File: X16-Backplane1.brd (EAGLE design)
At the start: 131.3 x 109.7 mm, 26 parts, among them J1 CONN_PXC-8-RA-1778683, J12 282837-3, J13 282837-3, J2 CONN_ET60S-D04-3-08-D04-X-R1-S, J3 HTST-110-04-L-D-RA, J4 CLT-110-01-F-D, U2 TRANS_ULN2003AD

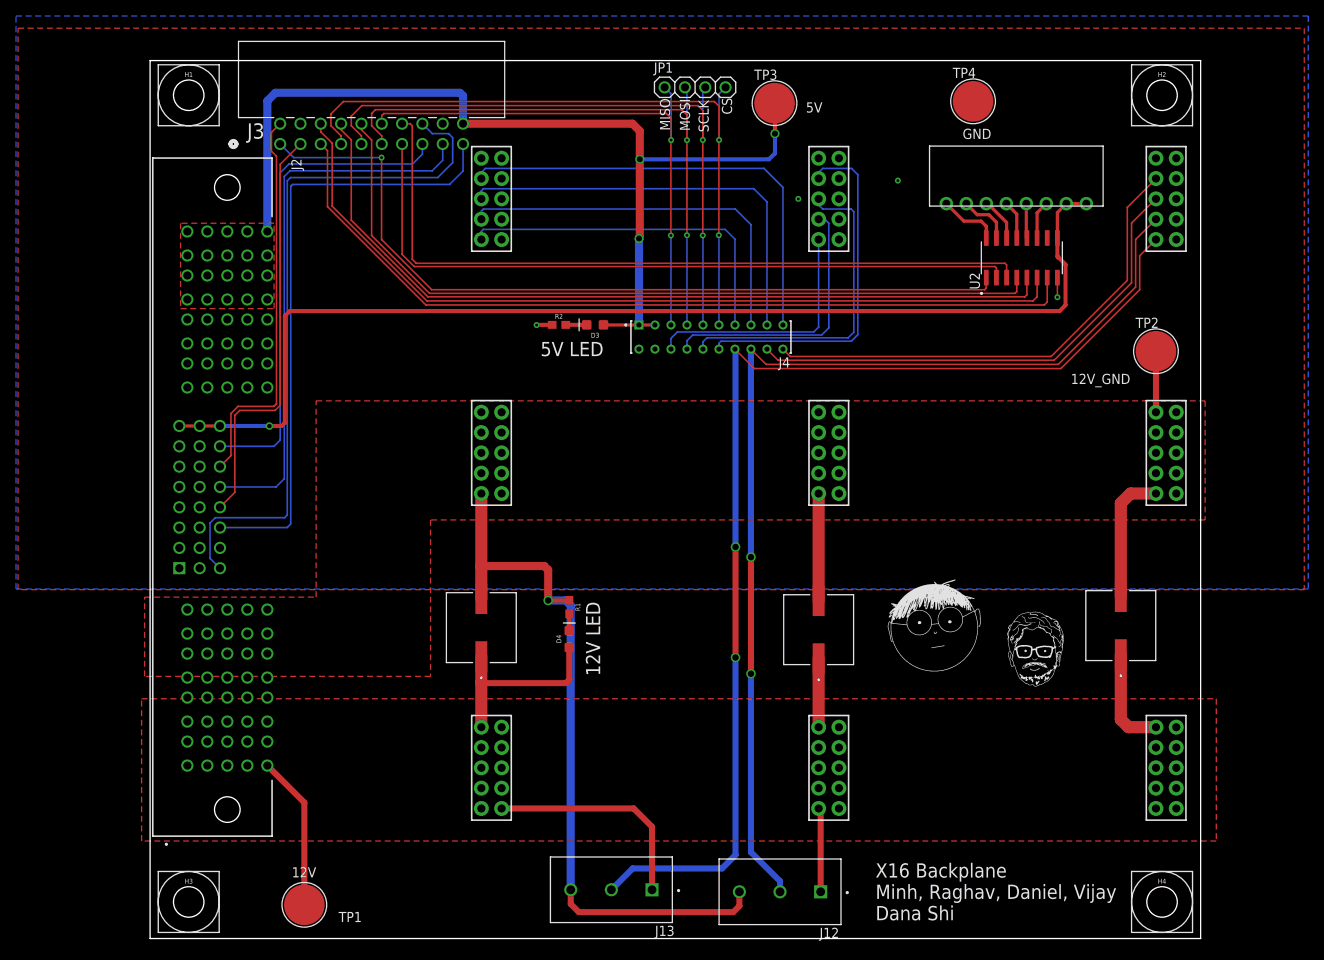
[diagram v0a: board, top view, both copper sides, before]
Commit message: Revert "Minh Update 4"
This reverts commit 6540dcb78246fca95661c726553611ac5071b16d.
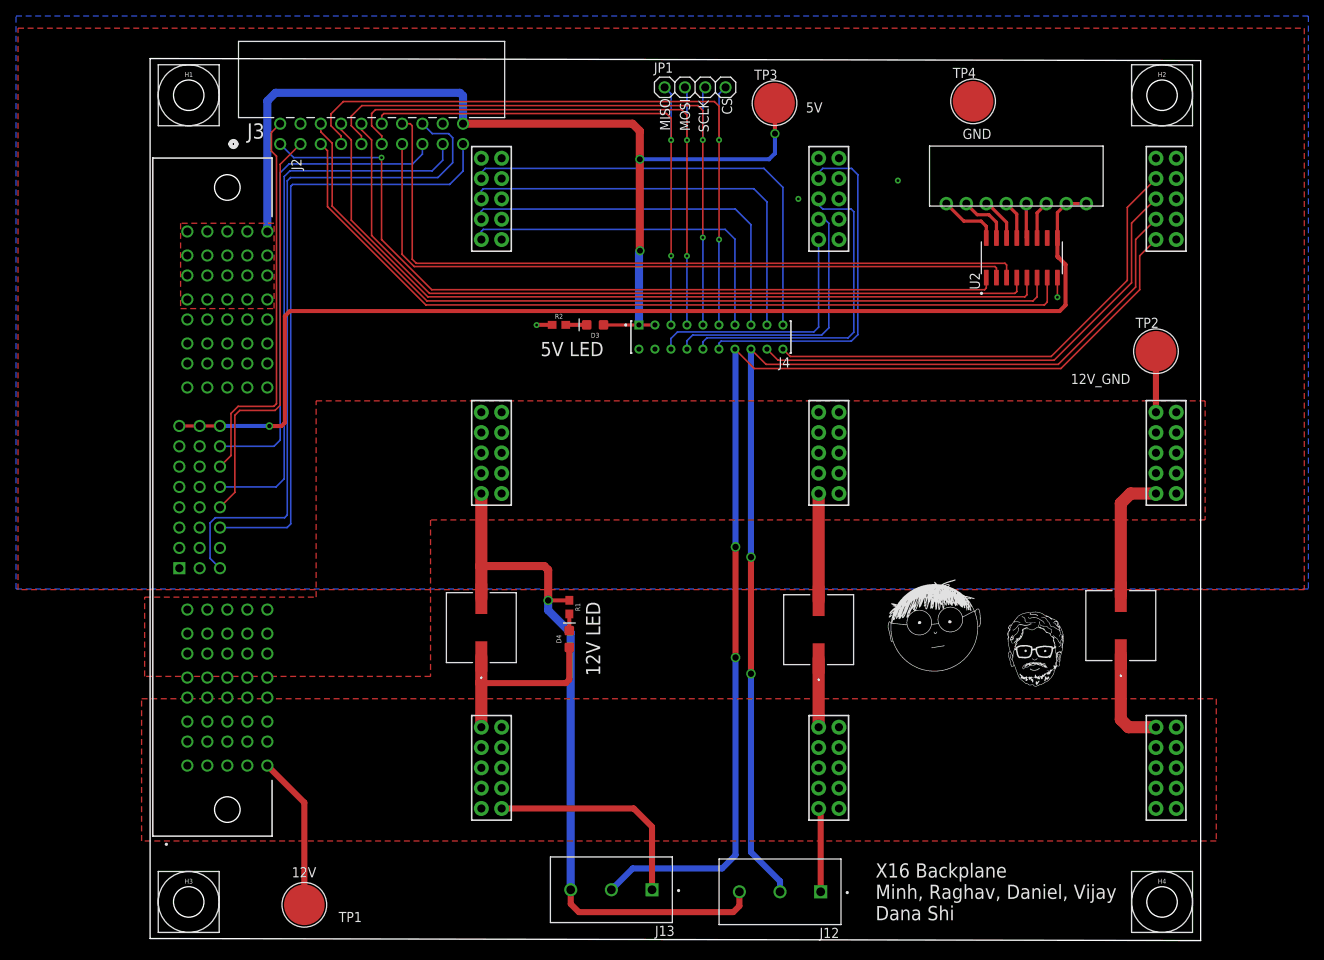
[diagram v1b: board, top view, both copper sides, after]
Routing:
- net 12V_GND: track 129.8 -> 128.5 mm
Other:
- board size 131.3 x 109.7 mm -> 131.3 x 110.3 mm
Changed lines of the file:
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@@
 <board>
 <plain>
-<wire x1="0" y1="0" x2="131.318" y2="0" width="0" layer="20"/>
-<wire x1="131.318" y1="0" x2="131.318" y2="109.746" width="0" layer="20"/>
-<wire x1="131.318" y1="109.746" x2="0" y2="109.746" width="0" layer="20"/>
-<wire x1="0" y1="109.746" x2="0" y2="0" width="0" layer="20"/>
+<wire x1="0" y1="0" x2="131.318" y2="-0.254" width="0" layer="20"/>
+<wire x1="131.318" y1="-0.254" x2="131.318" y2="109.746" width="0" layer="20"/>
+<wire x1="131.318" y1="109.746" x2="0" y2="110" width="0" layer="20"/>
+<wire x1="0" y1="110" x2="0" y2="0" width="0" layer="20"/>
 <polygon width="0.4064" layer="29">
 <vertex x="23.368" y="56.388"/>
@@
 <wire x1="41.402" y1="55.626" x2="41.402" y2="46.5582" width="1.524" layer="1"/>
 <wire x1="125.73" y1="65.786" x2="125.73" y2="73.406" width="0.762" layer="1"/>
-<wire x1="52.578" y1="6.096" x2="52.578" y2="41.6306" width="1.016" layer="16"/>
+<wire x1="52.578" y1="6.096" x2="52.578" y2="38.2016" width="1.016" layer="16"/>
+<wire x1="49.7586" y1="41.021" x2="49.7586" y2="42.2656" width="1.016" layer="16"/>
 <via x="49.7586" y="42.2656" extent="1-16" drill="0.8"/>
-<wire x1="52.578" y1="41.6306" x2="51.943" y2="42.2656" width="1.016" layer="16"/>
-<wire x1="49.7586" y1="42.2656" x2="51.943" y2="42.2656" width="1.016" layer="16"/>
+<wire x1="52.578" y1="38.2016" x2="49.7586" y2="41.021" width="1.016" layer="16"/>
 <wire x1="49.7586" y1="42.2656" x2="49.7586" y2="46.0756" width="1.016" layer="1"/>
 <wire x1="49.7586" y1="46.0756" x2="49.276" y2="46.5582" width="1.016" layer="1"/>
@@
 <wire x1="61.214" y1="100.9396" x2="61.214" y2="97.409" width="1.016" layer="1"/>
 <via x="61.214" y="97.409" extent="1-16" drill="0.75"/>
-<wire x1="61.214" y1="97.409" x2="61.214" y2="87.6046" width="1.016" layer="1"/>
-<wire x1="61.214" y1="87.6046" x2="61.1124" y2="87.503" width="1.016" layer="1"/>
-<via x="61.1124" y="87.503" extent="1-16" drill="0.75"/>
-<wire x1="61.1124" y1="87.503" x2="61.1124" y2="76.7024" width="1.016" layer="16"/>
+<wire x1="61.214" y1="97.409" x2="61.214" y2="86.0044" width="1.016" layer="1"/>
+<wire x1="61.214" y1="86.0044" x2="61.2394" y2="85.979" width="1.016" layer="1"/>
+<via x="61.2394" y="85.979" extent="1-16" drill="0.75"/>
+<wire x1="61.2394" y1="85.979" x2="61.1124" y2="85.852" width="1.016" layer="16"/>
+<wire x1="61.1124" y1="85.852" x2="61.1124" y2="76.7024" width="1.016" layer="16"/>
 <wire x1="61.1124" y1="76.7024" x2="61.104" y2="76.694" width="1.016" layer="16"/>
 <wire x1="61.214" y1="97.409" x2="77.3684" y2="97.409" width="0.508" layer="16"/>
@@
 <contactref element="J4" pad="05"/>
 <contactref element="J3" pad="12"/>
-<wire x1="65.104" y1="76.694" x2="65.104" y2="87.8802" width="0.2032" layer="16"/>
-<wire x1="65.104" y1="87.8802" x2="65.1002" y2="87.884" width="0.2032" layer="16"/>
-<via x="65.1002" y="87.884" extent="1-16" drill="0.35"/>
-<wire x1="65.1002" y1="99.7712" x2="65.1256" y2="99.7966" width="0.2032" layer="1"/>
-<wire x1="65.1002" y1="99.7712" x2="65.1002" y2="87.884" width="0.2032" layer="1"/>
+<wire x1="65.104" y1="76.694" x2="65.104" y2="85.3224" width="0.2032" layer="16"/>
+<wire x1="65.104" y1="85.3224" x2="65.1256" y2="85.344" width="0.2032" layer="16"/>
+<via x="65.1256" y="85.344" extent="1-16" drill="0.35"/>
+<wire x1="65.1256" y1="85.344" x2="65.1256" y2="99.7966" width="0.2032" layer="1"/>
 <wire x1="65.1256" y1="99.7966" x2="65.1256" y2="102.5398" width="0.2032" layer="1"/>
 <wire x1="65.1256" y1="102.5398" x2="64.5414" y2="103.124" width="0.2032" layer="1"/>
@@
 <contactref element="J4" pad="07"/>
 <contactref element="J3" pad="11"/>
-<wire x1="67.104" y1="76.694" x2="67.104" y2="87.9066" width="0.2032" layer="16"/>
-<wire x1="67.104" y1="87.9066" x2="67.1068" y2="87.9094" width="0.2032" layer="16"/>
-<via x="67.1068" y="87.9094" extent="1-16" drill="0.35"/>
-<wire x1="67.1068" y1="87.9094" x2="67.1068" y2="99.7966" width="0.2032" layer="1"/>
+<wire x1="67.104" y1="76.694" x2="67.104" y2="85.3158" width="0.2032" layer="16"/>
+<wire x1="67.104" y1="85.3158" x2="67.1068" y2="85.3186" width="0.2032" layer="16"/>
+<via x="67.1068" y="85.3186" extent="1-16" drill="0.35"/>
+<wire x1="67.1068" y1="85.3186" x2="67.1068" y2="99.7966" width="0.2032" layer="1"/>
 <wire x1="67.1068" y1="99.7966" x2="67.1068" y2="102.9462" width="0.2032" layer="1"/>
 <wire x1="67.1068" y1="102.9462" x2="66.4464" y2="103.6066" width="0.2032" layer="1"/>
@@
 <contactref element="J4" pad="09"/>
 <contactref element="J3" pad="9"/>
-<wire x1="69.104" y1="76.694" x2="69.104" y2="87.868" width="0.2032" layer="16"/>
-<wire x1="69.104" y1="87.868" x2="69.088" y2="87.884" width="0.2032" layer="16"/>
-<via x="69.088" y="87.884" extent="1-16" drill="0.35"/>
-<wire x1="69.088" y1="87.884" x2="69.088" y2="99.822" width="0.2032" layer="1"/>
+<wire x1="69.104" y1="76.694" x2="69.104" y2="87.614" width="0.2032" layer="16"/>
+<wire x1="69.104" y1="87.614" x2="69.088" y2="87.63" width="0.2032" layer="16"/>
+<via x="69.088" y="87.63" extent="1-16" drill="0.35"/>
+<wire x1="69.088" y1="87.63" x2="69.088" y2="99.822" width="0.2032" layer="1"/>
 <wire x1="69.088" y1="99.822" x2="69.088" y2="103.505" width="0.2032" layer="1"/>
 <wire x1="69.088" y1="103.505" x2="68.4784" y2="104.1146" width="0.2032" layer="1"/>
@@
 <contactref element="J4" pad="11"/>
 <contactref element="J3" pad="7"/>
-<wire x1="71.104" y1="76.694" x2="71.104" y2="87.9" width="0.2032" layer="16"/>
-<wire x1="71.104" y1="87.9" x2="71.0946" y2="87.9094" width="0.2032" layer="16"/>
-<via x="71.0946" y="87.9094" extent="1-16" drill="0.35"/>
-<wire x1="71.0946" y1="99.7966" x2="71.12" y2="99.822" width="0.2032" layer="1"/>
-<wire x1="71.0946" y1="99.7966" x2="71.0946" y2="87.9094" width="0.2032" layer="1"/>
+<wire x1="71.104" y1="76.694" x2="71.104" y2="87.36" width="0.2032" layer="16"/>
+<wire x1="71.104" y1="87.36" x2="71.12" y2="87.376" width="0.2032" layer="16"/>
+<via x="71.12" y="87.376" extent="1-16" drill="0.35"/>
+<wire x1="71.12" y1="87.376" x2="71.12" y2="99.822" width="0.2032" layer="1"/>
 <wire x1="71.12" y1="99.822" x2="71.12" y2="104.0384" width="0.2032" layer="1"/>
 <wire x1="70.5358" y1="104.6226" x2="71.12" y2="104.0384" width="0.2032" layer="1"/>

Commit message: Minh Update 4
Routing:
- net 12V_GND: track 128.5 -> 129.8 mm
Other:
- board size 131.3 x 110.3 mm -> 131.3 x 109.7 mm
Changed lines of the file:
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@@
 <board>
 <plain>
-<wire x1="0" y1="0" x2="131.318" y2="-0.254" width="0" layer="20"/>
-<wire x1="131.318" y1="-0.254" x2="131.318" y2="109.746" width="0" layer="20"/>
-<wire x1="131.318" y1="109.746" x2="0" y2="110" width="0" layer="20"/>
-<wire x1="0" y1="110" x2="0" y2="0" width="0" layer="20"/>
+<wire x1="0" y1="0" x2="131.318" y2="0" width="0" layer="20"/>
+<wire x1="131.318" y1="0" x2="131.318" y2="109.746" width="0" layer="20"/>
+<wire x1="131.318" y1="109.746" x2="0" y2="109.746" width="0" layer="20"/>
+<wire x1="0" y1="109.746" x2="0" y2="0" width="0" layer="20"/>
 <polygon width="0.4064" layer="29">
 <vertex x="23.368" y="56.388"/>
@@
 <wire x1="41.402" y1="55.626" x2="41.402" y2="46.5582" width="1.524" layer="1"/>
 <wire x1="125.73" y1="65.786" x2="125.73" y2="73.406" width="0.762" layer="1"/>
-<wire x1="52.578" y1="6.096" x2="52.578" y2="38.2016" width="1.016" layer="16"/>
-<wire x1="49.7586" y1="41.021" x2="49.7586" y2="42.2656" width="1.016" layer="16"/>
+<wire x1="52.578" y1="6.096" x2="52.578" y2="41.6306" width="1.016" layer="16"/>
 <via x="49.7586" y="42.2656" extent="1-16" drill="0.8"/>
-<wire x1="52.578" y1="38.2016" x2="49.7586" y2="41.021" width="1.016" layer="16"/>
+<wire x1="52.578" y1="41.6306" x2="51.943" y2="42.2656" width="1.016" layer="16"/>
+<wire x1="49.7586" y1="42.2656" x2="51.943" y2="42.2656" width="1.016" layer="16"/>
 <wire x1="49.7586" y1="42.2656" x2="49.7586" y2="46.0756" width="1.016" layer="1"/>
 <wire x1="49.7586" y1="46.0756" x2="49.276" y2="46.5582" width="1.016" layer="1"/>
@@
 <wire x1="61.214" y1="100.9396" x2="61.214" y2="97.409" width="1.016" layer="1"/>
 <via x="61.214" y="97.409" extent="1-16" drill="0.75"/>
-<wire x1="61.214" y1="97.409" x2="61.214" y2="86.0044" width="1.016" layer="1"/>
-<wire x1="61.214" y1="86.0044" x2="61.2394" y2="85.979" width="1.016" layer="1"/>
-<via x="61.2394" y="85.979" extent="1-16" drill="0.75"/>
-<wire x1="61.2394" y1="85.979" x2="61.1124" y2="85.852" width="1.016" layer="16"/>
-<wire x1="61.1124" y1="85.852" x2="61.1124" y2="76.7024" width="1.016" layer="16"/>
+<wire x1="61.214" y1="97.409" x2="61.214" y2="87.6046" width="1.016" layer="1"/>
+<wire x1="61.214" y1="87.6046" x2="61.1124" y2="87.503" width="1.016" layer="1"/>
+<via x="61.1124" y="87.503" extent="1-16" drill="0.75"/>
+<wire x1="61.1124" y1="87.503" x2="61.1124" y2="76.7024" width="1.016" layer="16"/>
 <wire x1="61.1124" y1="76.7024" x2="61.104" y2="76.694" width="1.016" layer="16"/>
 <wire x1="61.214" y1="97.409" x2="77.3684" y2="97.409" width="0.508" layer="16"/>
@@
 <contactref element="J4" pad="05"/>
 <contactref element="J3" pad="12"/>
-<wire x1="65.104" y1="76.694" x2="65.104" y2="85.3224" width="0.2032" layer="16"/>
-<wire x1="65.104" y1="85.3224" x2="65.1256" y2="85.344" width="0.2032" layer="16"/>
-<via x="65.1256" y="85.344" extent="1-16" drill="0.35"/>
-<wire x1="65.1256" y1="85.344" x2="65.1256" y2="99.7966" width="0.2032" layer="1"/>
+<wire x1="65.104" y1="76.694" x2="65.104" y2="87.8802" width="0.2032" layer="16"/>
+<wire x1="65.104" y1="87.8802" x2="65.1002" y2="87.884" width="0.2032" layer="16"/>
+<via x="65.1002" y="87.884" extent="1-16" drill="0.35"/>
+<wire x1="65.1002" y1="99.7712" x2="65.1256" y2="99.7966" width="0.2032" layer="1"/>
+<wire x1="65.1002" y1="99.7712" x2="65.1002" y2="87.884" width="0.2032" layer="1"/>
 <wire x1="65.1256" y1="99.7966" x2="65.1256" y2="102.5398" width="0.2032" layer="1"/>
 <wire x1="65.1256" y1="102.5398" x2="64.5414" y2="103.124" width="0.2032" layer="1"/>
@@
 <contactref element="J4" pad="07"/>
 <contactref element="J3" pad="11"/>
-<wire x1="67.104" y1="76.694" x2="67.104" y2="85.3158" width="0.2032" layer="16"/>
-<wire x1="67.104" y1="85.3158" x2="67.1068" y2="85.3186" width="0.2032" layer="16"/>
-<via x="67.1068" y="85.3186" extent="1-16" drill="0.35"/>
-<wire x1="67.1068" y1="85.3186" x2="67.1068" y2="99.7966" width="0.2032" layer="1"/>
+<wire x1="67.104" y1="76.694" x2="67.104" y2="87.9066" width="0.2032" layer="16"/>
+<wire x1="67.104" y1="87.9066" x2="67.1068" y2="87.9094" width="0.2032" layer="16"/>
+<via x="67.1068" y="87.9094" extent="1-16" drill="0.35"/>
+<wire x1="67.1068" y1="87.9094" x2="67.1068" y2="99.7966" width="0.2032" layer="1"/>
 <wire x1="67.1068" y1="99.7966" x2="67.1068" y2="102.9462" width="0.2032" layer="1"/>
 <wire x1="67.1068" y1="102.9462" x2="66.4464" y2="103.6066" width="0.2032" layer="1"/>
@@
 <contactref element="J4" pad="09"/>
 <contactref element="J3" pad="9"/>
-<wire x1="69.104" y1="76.694" x2="69.104" y2="87.614" width="0.2032" layer="16"/>
-<wire x1="69.104" y1="87.614" x2="69.088" y2="87.63" width="0.2032" layer="16"/>
-<via x="69.088" y="87.63" extent="1-16" drill="0.35"/>
-<wire x1="69.088" y1="87.63" x2="69.088" y2="99.822" width="0.2032" layer="1"/>
+<wire x1="69.104" y1="76.694" x2="69.104" y2="87.868" width="0.2032" layer="16"/>
+<wire x1="69.104" y1="87.868" x2="69.088" y2="87.884" width="0.2032" layer="16"/>
+<via x="69.088" y="87.884" extent="1-16" drill="0.35"/>
+<wire x1="69.088" y1="87.884" x2="69.088" y2="99.822" width="0.2032" layer="1"/>
 <wire x1="69.088" y1="99.822" x2="69.088" y2="103.505" width="0.2032" layer="1"/>
 <wire x1="69.088" y1="103.505" x2="68.4784" y2="104.1146" width="0.2032" layer="1"/>
@@
 <contactref element="J4" pad="11"/>
 <contactref element="J3" pad="7"/>
-<wire x1="71.104" y1="76.694" x2="71.104" y2="87.36" width="0.2032" layer="16"/>
-<wire x1="71.104" y1="87.36" x2="71.12" y2="87.376" width="0.2032" layer="16"/>
-<via x="71.12" y="87.376" extent="1-16" drill="0.35"/>
-<wire x1="71.12" y1="87.376" x2="71.12" y2="99.822" width="0.2032" layer="1"/>
+<wire x1="71.104" y1="76.694" x2="71.104" y2="87.9" width="0.2032" layer="16"/>
+<wire x1="71.104" y1="87.9" x2="71.0946" y2="87.9094" width="0.2032" layer="16"/>
+<via x="71.0946" y="87.9094" extent="1-16" drill="0.35"/>
+<wire x1="71.0946" y1="99.7966" x2="71.12" y2="99.822" width="0.2032" layer="1"/>
+<wire x1="71.0946" y1="99.7966" x2="71.0946" y2="87.9094" width="0.2032" layer="1"/>
 <wire x1="71.12" y1="99.822" x2="71.12" y2="104.0384" width="0.2032" layer="1"/>
 <wire x1="70.5358" y1="104.6226" x2="71.12" y2="104.0384" width="0.2032" layer="1"/>
